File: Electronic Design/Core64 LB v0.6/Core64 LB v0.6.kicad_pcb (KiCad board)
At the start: 2 copper layers, 85 x 170 mm, 153 parts, among them IC1 LP3961EMP-5.0, IC2 TPS7A0533PDBVR, J1 SSW-116-22-F-S-VS‎, J10 TSM-106-03-T-DV‎, J11 HEADER_8-PIN_0.1, J12 TEENSY Cur. Mon., J13 Core Cur. Mon., J14 HEADER_11-PIN_0.1, J17 LED Cur. Mon., J2 SSW-116-22-F-S-VS‎, J3 Conn_01x08_Female, J4 PRG, J5 HEADER_8-PIN_0.1, J6 HEADER_8-PIN_0.1, J7 S03B-PASK-2_LF__SN_, J8 5V0 Cur. Mon., J9 3V3 Cur. Mon., Q1 MCC_SL3401A, Q10 MMBT4401LT1G, Q11 MMBT4403LT1G, Q12 MMBT4401LT1G, Q13 MMBT4403LT1G, Q14 MMBT4401LT1G, Q15 MMBT4403LT1G, Q16 MMBT4401LT1G, Q17 MMBT4403LT1G, Q18 MMBT4401LT1G, Q19 MMBT4403LT1G, Q2 MMBT4403LT1G, Q20 MMBT4401LT1G, Q21 MMBT4403LT1G, Q22 MMBT4401LT1G, Q3 MMBT4401LT1G, Q4 MMBT4403LT1G, Q5 MMBT4401LT1G, Q6 MMBT4403LT1G, Q7 MMBT4401LT1G, Q8 Q_NMOS_DGS_NVTR4503NT1G, Q9 MMBT4403LT1G, SW1 JS102011SAQN, U1 74HC02, U2 Teensy3.2, U3 SN74LV1T125DBVR, U4 M24C02-RMN, U5 74HC238, U6 Micro_LiPo_Charger, U7 LM393, U8 Adafruit_3.2_TFT_1743, X1 SSW-104-22-L-S-VS, X2 Header_9-PIN_0.1, X3 QWIIC, X4 SAO_conn_SFH11-NBPC-D03-ST-BK

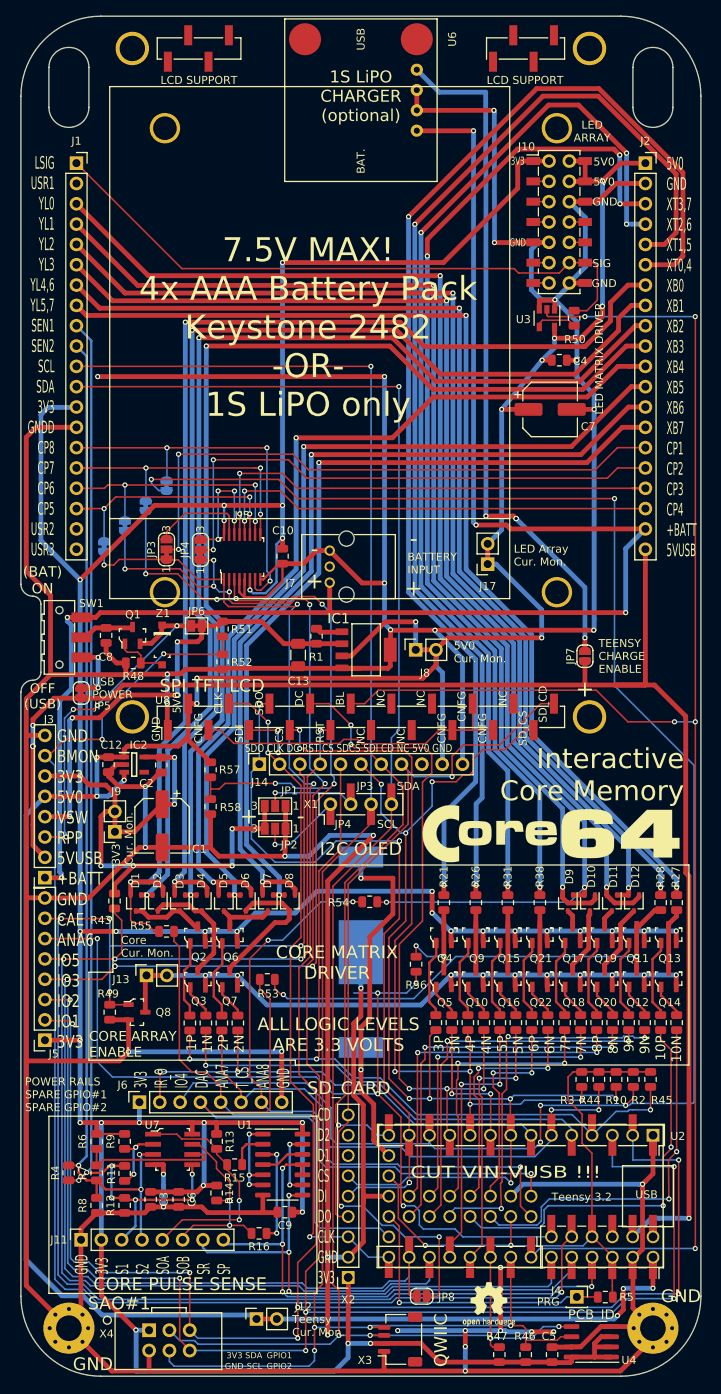
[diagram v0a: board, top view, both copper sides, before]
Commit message: APPLY LOGIC BOARD V0.5 FIXES NEEDED TO BE V0.6 U1 silk screen should be placed by pin 1 not pin 7 Check J1 and J2 labels so J1 is on the left, like it is for the Core Board Remove Header for old LED Matrix, since is no longer needed and it is in the way. RTC Notes on schematic, must add THREE things, typo change from TWO. Below JP5 Teensy Charge Enable is a rogue "+" on the silk screen Left of R56 is a dead-end trace stub. Doesn't hurt anything but it's not right. 6.8 Ohm Core Current Limit Resistors can move to 5%. JP1/2 for OLED should be JP1/2 on the OLED silk screen, not JP3/4 Silk screen, left header row, swap SEN1 and SEN2 text so they match to S1 and S2 correctly on the inner perimeter. Move to larger logo and other text on the backside Update silk screen for all boards with P/Ns, bare board. Move top row of TFT LCD support down 0.55mm. Add 470 resistor to gate of core array enable to limit current. Change I2C pull-up resistors from 2.2K to 1.2K 20% (E12 series is most common, and values overlap) Remove two dead-end GND (BAT-) traces between/below Teensy 25/26, and over to QWIIC. Add I2C series resistors 68 Ohm at output of Teensy. Move the 470uF LED 5V0 capacitor, down to be between 5V0 Cur Mon and Teensy Charge enable jumpers, out of the way of the batteries. New stylus position is on left, so the 3V3 capacitor needs to move in a few mm to allow it to pass through. Provide thru-holes for alternate 3.3V and 5V bulk capacitor options. Propagation through sense logic chips was 200ns, reduce PU to 1K2 and remove inline 10Ks. Now 50ns. Voltage divider and other resistors, consolidated to 10K resistors. Keep the two 10K resistors on the 5V0 MON. Add a SJ in series to isolate from Hall Switches. Replace the inline 10K resistors in the all optional Voltage Monitoring lines with closed SJs instead. Clean-up all the horz/vert traces left from removing LED drive header and relocating the driver and 5V0 cap Part substitutions Data sheet updates
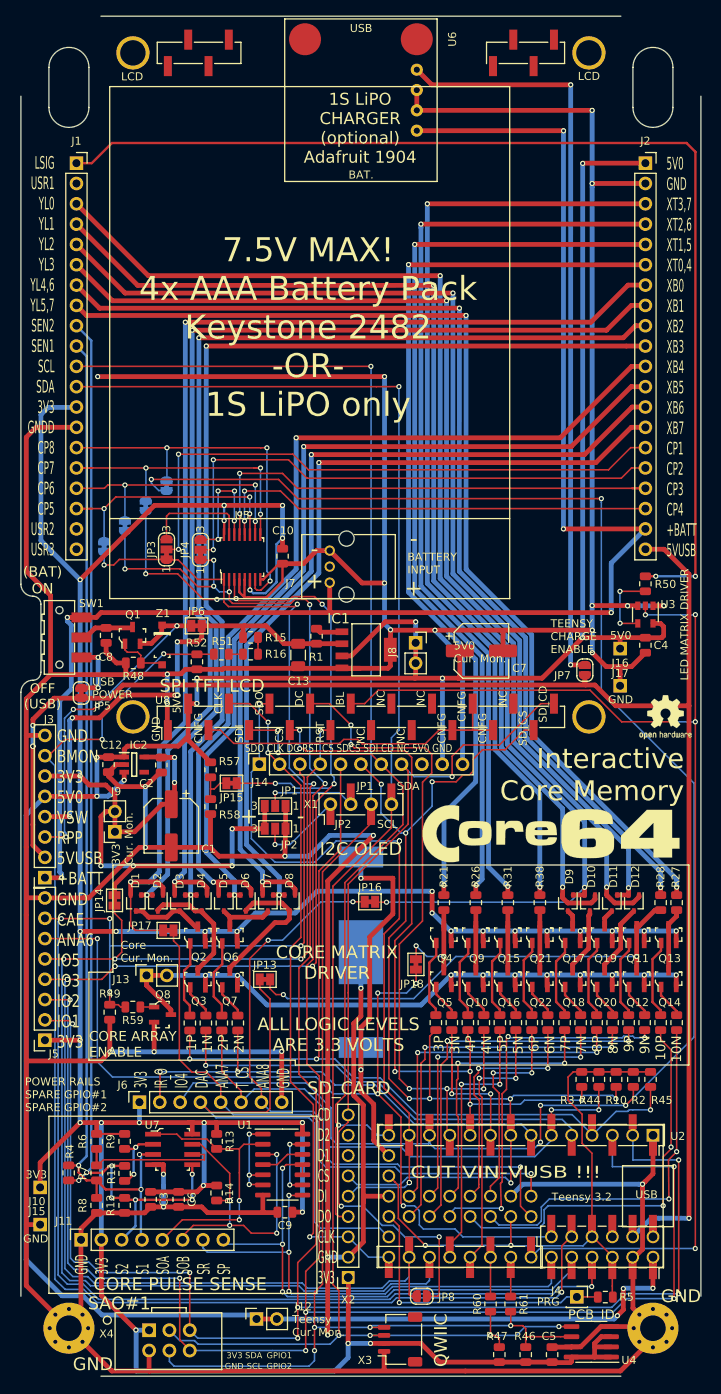
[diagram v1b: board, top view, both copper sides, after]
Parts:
- removed R43, R53, R54, R55, R56: 10k, Resistor_SMD:R_0805_2012Metric
- added J15: Conn_01x01_Male, Connector_PinHeader_2.54mm:PinHeader_1x01_P2.54mm_Vertical_No_Registration, F.Cu at (-40.1, 108.5)
- added J16: Conn_01x01_Male, Connector_PinHeader_2.54mm:PinHeader_1x01_P2.54mm_Vertical_No_Registration, F.Cu at (32.4, 36.5)
- added JP13: RR0 MON, Jumper:SolderJumper-2_P1.3mm_Bridged_Pad1.0x1.5mm, F.Cu at (-12.0, 77.9)
- added JP14: 3V3 MON, Jumper:SolderJumper-2_P1.3mm_Bridged_Pad1.0x1.5mm, F.Cu at (-30.8, 68.0)
- added JP15: 5V0 MON, Jumper:SolderJumper-2_P1.3mm_Bridged_Pad1.0x1.5mm, F.Cu at (-16.2, 53.4)
- added JP16: LR0 MON, Jumper:SolderJumper-2_P1.3mm_Bridged_Pad1.0x1.5mm, F.Cu at (1.12, 68.2)
- added JP17: BC0 MON, Jumper:SolderJumper-2_P1.3mm_Bridged_Pad1.0x1.5mm, F.Cu at (-24.1, 71.8)
- added JP18: TC0 MON, Jumper:SolderJumper-2_P1.3mm_Bridged_Pad1.0x1.5mm, F.Cu at (6.88, 76.0)
- added R59: 470, Resistor_SMD:R_0805_2012Metric, F.Cu at (-28.5, 81.3)
- added R60: 68, Resistor_SMD:R_0805_2012Metric, F.Cu at (16.2, 118.5)
- added R61: 68, Resistor_SMD:R_0805_2012Metric, F.Cu at (18.7, 118.5)
- J10: value TSM-106-03-T-DV‎ -> Conn_01x01_Male; footprint Connector_PinHeader_2.54mm:PinHeader_2x07_P2.54mm_Vertical_SMD_and_TH -> Connector_PinHeader_2.54mm:PinHeader_1x01_P2.54mm_Vertical_No_Registration
- J17: value LED Cur. Mon. -> Conn_01x01_Male; footprint Connector_PinSocket_2.54mm:PinSocket_1x02_P2.54mm_Vertical -> Connector_PinHeader_2.54mm:PinHeader_1x01_P2.54mm_Vertical_No_Registration
- L2: footprint Core_Memory_8x8_Array:Core64_Logo -> Core_Memory_8x8_Array:Core64_Logo_9mm_tall
- R13, R14: value 10k -> 1K2
- R15, R16: value 10k -> 10K
- R21, R26, R27, R28, R31, R38: value 6R8-1% -> 6R8-5%
- R46, R47: value 2K2 -> 1K2
- R51: value 33k -> 10K
- R52, R57, R58: value 11k -> 10K
- moved J10 110.9 mm to (-40.1, 103.9), turned to 270 degrees
- moved L4 76.6 mm to (38.1, 45.1)
- moved R16 72.4 mm to (-13.8, 37.2)
- moved R15 65.9 mm to (-13.8, 35.1), turned to 0 degrees
- moved U3 39.0 mm to (35.6, 32.3)
- moved C4 37.2 mm to (35.6, 36.1), turned to 270 degrees
- moved R50 34.4 mm to (35.6, 28.4)
- moved C7 31.4 mm to (15.1, 36.8)
- moved J17 22.5 mm to (32.4, 41.2), turned to 270 degrees
- moved L2 11.0 mm to (0.00, -22.0)
- moved Q8 3.21 mm to (-24.8, 82.3)
- moved R52 3.20 mm to (-20.5, 38.2)
- moved R51 3.15 mm to (-17.4, 37.2), turned to 180 degrees
- moved JP7 1.74 mm to (28.0, 39.2)
- moved C1 1.15 mm to (-23.7, 58.7)
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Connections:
- J1 pad 10: SENSE2 -> SENSE1
- J1 pad 9: SENSE1 -> SENSE2
- J11 pad 3: SENSE1 -> SENSE2
- J11 pad 4: SENSE2 -> SENSE1
- J17 pad 1: 5V0 -> -BATT
- J5 pad 4: 5V0_MON -> HS3
- JP11 pad 1: 5V0_MON -> HS3
- JP8 pad 1: 5V0_MON -> HS3
- Q8 pad 1: OLED_SPI_DC -> Net-(Q8-Pad1)
- R11 pad 2: SENSE1 -> SENSE2
- R12 pad 1: SENSE1 -> SENSE2
- R15 pad 1: Net-(R15-Pad1) -> +VSW
- R15 pad 2: SENSE_OUT_A -> Net-(R15-Pad2)
- R16 pad 1: Net-(R16-Pad1) -> Net-(R15-Pad2)
- R16 pad 2: SENSE_OUT_B -> Net-(R16-Pad2)
- R4 pad 1: SENSE1 -> SENSE2
- R4 pad 2: SENSE2 -> SENSE1
- R51 pad 1: +VSW -> Net-(R16-Pad2)
- R7 pad 2: SENSE2 -> SENSE1
- R8 pad 1: SENSE2 -> SENSE1
- U1 pad 2: Net-(R15-Pad1) -> SENSE_OUT_A
- U1 pad 3: Net-(R16-Pad1) -> SENSE_OUT_B
- U2 pad 21: 5V0_MON -> HS3
- U2 pad 25: I2C_DATA -> Net-(R60-Pad2)
- U2 pad 26: I2C_CLOCK -> Net-(R61-Pad1)
- U5 pad 3: 5V0_MON -> HS3
- U7 pad 3: SENSE2 -> SENSE1
- U7 pad 5: SENSE1 -> SENSE2
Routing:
- net 5V0_MON: track 225.2 -> 5.00 mm, vias 11 -> 0
- net HS3: track 0.00 -> 218.9 mm, vias 0 -> 11
- net 3V3: track 577.1 -> 516.4 mm, vias 39 -> 38
- net LED_MATRIX_5V0_SIG: track 79.2 -> 138.2 mm, vias 0 -> 2
- net LED_MATRIX_3V3_SIG: track 203.9 -> 154.7 mm
- net XT0,4: track 150.8 -> 113.6 mm
- net -BATT: track 911.1 -> 879.6 mm, vias 33 -> 27
- net XT1,5: track 142.8 -> 114.0 mm
- net XT2,6: track 133.4 -> 116.4 mm, vias 4 -> 2
- net SENSE_OUT_B: track 24.3 -> 39.1 mm, vias 4 -> 6
- net Net-(R16-Pad1): track 12.9 -> 0.00 mm, vias 2 -> 0
- net SENSE2: track 128.9 -> 139.0 mm, vias 3 -> 7
- net SENSE1: track 139.0 -> 128.9 mm, vias 7 -> 3
- net I2C_DATA: track 232.7 -> 223.4 mm
- net I2C_CLOCK: track 231.1 -> 222.9 mm
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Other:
- board text added: ".io"
- board text added: "1S LiPO CHARGER (optional) Adafruit 1904"
- board text added: "DESC: Core64 Logic Board PCB P/N: 112-001 REV: 0.6 (2021-11-07) PCBA P/N: 112-000"
- board text added: "Designed by Andy Geppert www.MachineIdeas.com"
- board text added: "GND 3V3 S2 S1 SOA SOB SR SP"
- board text added: "JP1"
- board text added: "JP2"
- board text added: "LCD"
- board text added: "LSIG USR1 YL0 YL1 YL2 YL3 YL4,6 YL5,7 SEN2 SEN1 SCL SDA 3V3 GNDD CP8 CP7 CP6 CP5 USR2 USR3"
- board text removed: "1S LiPO CHARGER (optional)"
- board text removed: "Andy Geppert"
- board text removed: "GND 3V3 S1 S2 SOA SOB SR SP"
- board text removed: "JP3"
- board text removed: "JP4"
- board text removed: "LCD SUPPORT"
- board text removed: "LED ARRAY"
- board text removed: "LED Array Cur. Mon."
- board text removed: "LSIG USR1 YL0 YL1 YL2 YL3 YL4,6 YL5,7 SEN1 SEN2 SCL SDA 3V3 GNDD CP8 CP7 CP6 CP5 USR2 USR3"
- board text removed: "Part Number: Logic Board Revision: 0.5 Release Date: 2021-02-27"
- board text removed: "SIG"
- board text removed: "www.Core64.io"

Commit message: Revise LB V0.6, part substitutions, data sheet updates, clean up Ref. Des. to be in order and easier to find on the board in groups
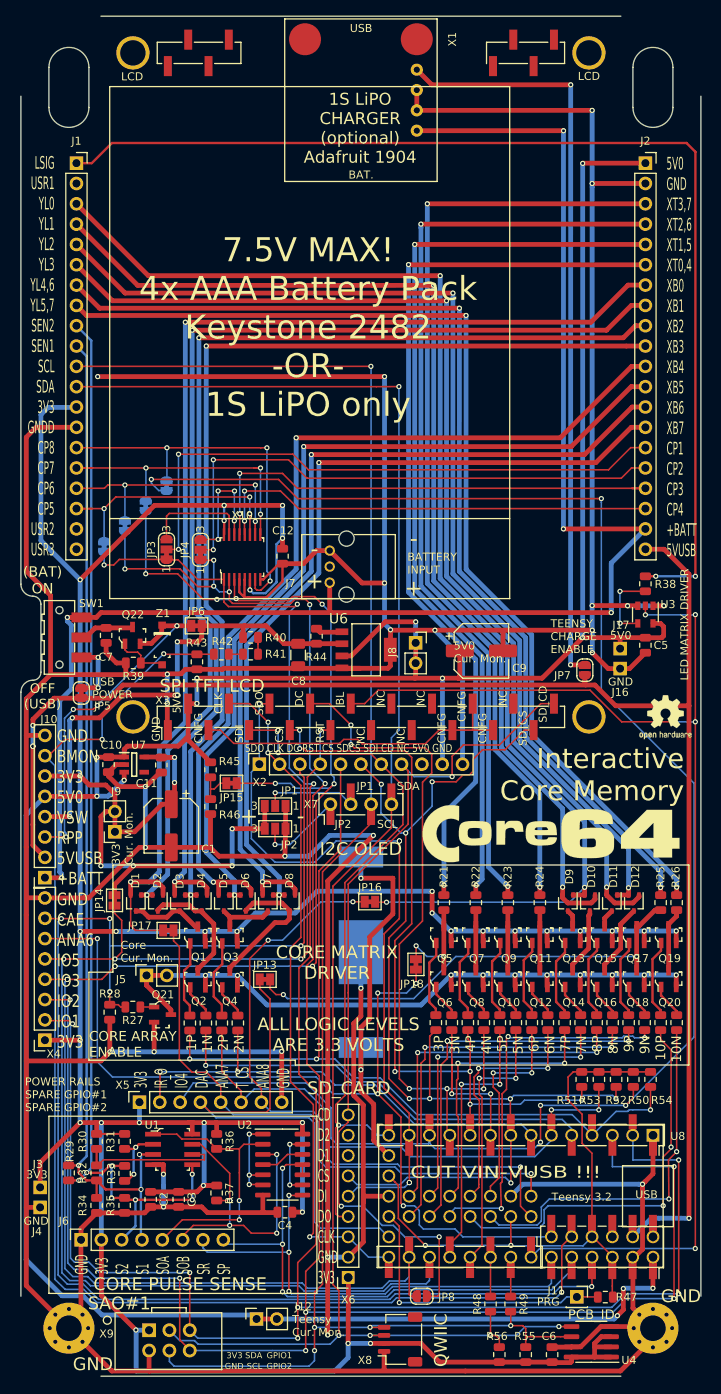
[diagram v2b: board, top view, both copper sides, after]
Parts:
- removed the J10 at (-40.1, 103.9)
- added J3: Conn_01x01_Male, Connector_PinHeader_2.54mm:PinHeader_1x01_P2.54mm_Vertical_No_Registration, F.Cu at (-40.1, 103.9)
- J10: renamed from J3; value Conn_01x08_Female -> CORE Cur. Mon.
- J5: renamed from J13; value Core Cur. Mon. -> CORE Cur. Mon.
- J6: renamed from J11; value HEADER_8-PIN_0.1 -> SENSE DEBUG
- Q21: renamed from Q8; value Q_NMOS_DGS_NVTR4503NT1G -> NVTR4503NT1G_NMOS_GSD
- Q22: renamed from Q1; value MCC_SL3401A -> MCC_SL3401A_PMOS_GSD
- U2: renamed from U1; value 74HC02 -> SN74HC02DR
- moved J17 2.15 mm to (32.4, 39.0)
- moved J4 2.15 mm to (-40.1, 106.4)
- renumbered C12 to C10, C2 to C11, C10 to C12, C3 to C2, C6 to C3, C9 to C4, C4 to C5, C5 to C6, C8 to C7, C13 to C8, C7 to C9, J4 to J11, J15 to J4, Q2 to Q1, Q16 to Q10, Q21 to Q11, Q22 to Q12, Q17 to Q13, Q18 to Q14, Q19 to Q15, Q20 to Q16, Q11 to Q17, Q12 to Q18, Q13 to Q19, Q3 to Q2, Q14 to Q20, Q6 to Q3, Q7 to Q4, Q4 to Q5, Q5 to Q6, Q9 to Q7, Q10 to Q8, Q15 to Q9, R17 to R1, R30 to R10, R36 to R11, R37 to R12, R39 to R13, R40 to R14, R41 to R15, R42 to R16, R34 to R17, R35 to R18, R32 to R19, R18 to R2, R33 to R20, R26 to R22, R31 to R23, R38 to R24, R28 to R25, R27 to R26, R59 to R27, R49 to R28, R4 to R29, R22 to R3, R6 to R30, R9 to R31, R7 to R32, R11 to R33, R8 to R34, R12 to R35, R13 to R36, R14 to R37, R50 to R38, R48 to R39, R23 to R4, R15 to R40, R16 to R41, R51 to R42, R52 to R43, R1 to R44, R57 to R45, R58 to R46, R5 to R47, R60 to R48, R61 to R49, R19 to R5, R2 to R50, R3 to R51, R10 to R52, R44 to R53, R45 to R54, R46 to R55, R47 to R56, R20 to R6, R24 to R7, R25 to R8, R29 to R9, U7 to U1, IC1 to U6, IC2 to U7, U2 to U8, U6 to X1, U5 to X10, J14 to X2, U8 to X3, J5 to X4, J6 to X5, X2 to X6, X1 to X7, X3 to X8, X4 to X9
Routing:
- net -BATT: track 879.6 -> 877.5 mm

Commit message: Refine LB v0.6 layout, KiCAD BOM updates, review schematic and PCB for release
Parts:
- J12: renamed from J10; value CORE Cur. Mon. -> Power Rails
- JP7: renamed from JP6; value Opt. Cur. Mon. -> Sys. Cur. Mon.
- moved J11 11.7 mm to (21.2, 35.6), turned to 90 degrees
- moved J10 11.3 mm to (21.2, 38.1), turned to 90 degrees
- moved L4 2.62 mm to (35.5, 45.6)
- moved C9 1.30 mm to (13.8, 36.8)
- renumbered J16 to J10, J17 to J11, J11 to J13, J12 to J14, JP9 to JP1, JP14 to JP10, JP13 to JP11, JP16 to JP12, JP17 to JP13, JP18 to JP14, JP1 to JP15, JP2 to JP16, JP3 to JP17, JP4 to JP18, JP10 to JP2, JP11 to JP3, JP12 to JP4, JP7 to JP5, JP5 to JP6, JP15 to JP9, U6 to U5, U7 to U6, U8 to U7, X10 to U8
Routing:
- net 5V0: track 353.7 -> 354.3 mm
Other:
- board text added: "DESC: Core64 Logic Board PCB P/N: 112-001 REV: 0.6 (2021-11-09) PCBA P/N: 112-000"
- board text added: "JP15"
- board text added: "JP16"
- board text added: "Sys. Cur. Mon."
- board text removed: "DESC: Core64 Logic Board PCB P/N: 112-001 REV: 0.6 (2021-11-07) PCBA P/N: 112-000"
- board text removed: "JP1"
- board text removed: "JP2"
